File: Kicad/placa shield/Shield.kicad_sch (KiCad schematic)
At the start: 22 parts, among them J1 HC-05 connector, J2 Digital/PWM, J3 Power, J4 Analog, J5 Digital/PWM, J6 Dimmer module, SW1 SW_Push, SW2 SW_Push, SW3 SW_Push, SW4 SW_Push, SW5 SW_DIP_x04, X3 ST-MORPHO-CN7, X4 ST-MORPHO-CN10

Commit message: previo a fabricación
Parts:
- removed R15, R16: 10k, Resistor_THT:R_Axial_DIN0207_L6.3mm_D2.5mm_P7.62mm_Horizontal, symbol Device:R
- removed SW3, SW4: SW_Push, Button_Switch_THT:SW_PUSH_6mm, symbol Switch:SW_Push
- RV1: value 1k -> 10k
- renumbered SW2 to Luz_OFF, SW1 to Luz_ON
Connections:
- net PA0 is gone; now on net A0: X3.28 (PA0)
- net PA1 is gone; now on net A1: X3.30 (PA1)
- net PA10 is gone; now on net 2: X4.33 (PA10)
- net PA2 is gone; now on net TX/1: X4.35 (PA2)
- net PA3 is gone; now on net RX/0: X4.37 (PA3)
- net PA9 is gone; now on net 8: X4.21 (PA9)
- net *10: now also X4.17 (PB6)
- net *11: now also X4.15 (PA7)
- net *3: now also X4.31 (PB3)
- net *5: now also X4.27 (PB4)
- net *6: now also X4.25 (PB10)
- net *9: now also X4.19 (PC7)
- net +3V3: now also Luz_OFF.2, Luz_ON.2, RV1.1, SW5.1, SW5.2, SW5.3, SW5.4
- net +5V: now also X3.18 (+5V); no longer Luz_OFF.2, Luz_ON.2, RV1.1, SW5.1, SW5.2, SW5.3, SW5.4
- net 12: now also X4.13 (PA6)
- net 13: now also X4.11 (PA5)
- net 4: now also X4.29 (PB5)
- net 7: now also X4.23 (PA8)
- net A2: now also X3.32 (PA4)
- net A3: now also X3.34 (PB0)
- net AGND: no longer X3.20 (GND), X3.22 (GND), X3.8 (GND), X4.20 (GND)
- net AREF: now also X4.7 (AVDD)
- net GND: now also X3.20 (GND), X3.22 (GND)
- net IOREF: now also X3.12 (IOREF)
- net SCL/A5: now also X3.38 (PC0/PB8), X4.3 (PB8)
- net SDA/A4: now also X3.36 (PC1/PB9), X4.5 (PB9)
- net VCC: now also X3.24 (VIN)
- net ~{RESET}: now also X3.14 (RESET)
- net +5V0: no longer names the net of X3.6 (E5V)
- net PA11: no longer names the net of X4.14 (PA11)
- net PA12: no longer names the net of X4.12 (PA12)
- net PB12: no longer names the net of X4.16 (PB12)
- net PB13: no longer names the net of X4.30 (PB13)
- net PB14: no longer names the net of X4.28 (PB14)
- net PB15: no longer names the net of X4.26 (PB15)
- net U5V: no longer names the net of X4.8 (U5V)
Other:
- moved on the sheet: RV1, X4

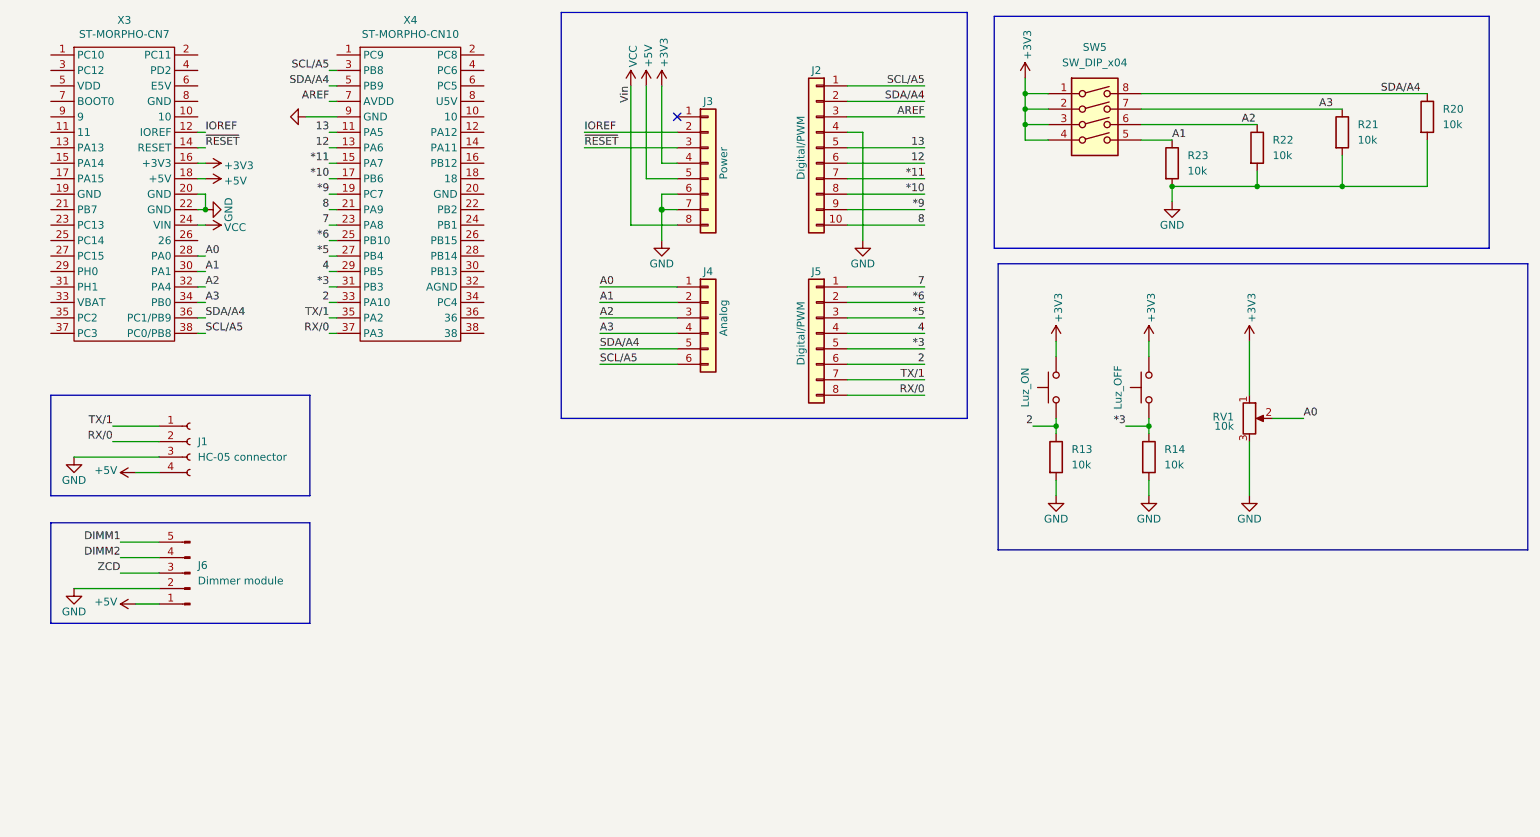
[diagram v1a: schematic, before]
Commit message: esquema shield actualizado con ínout final
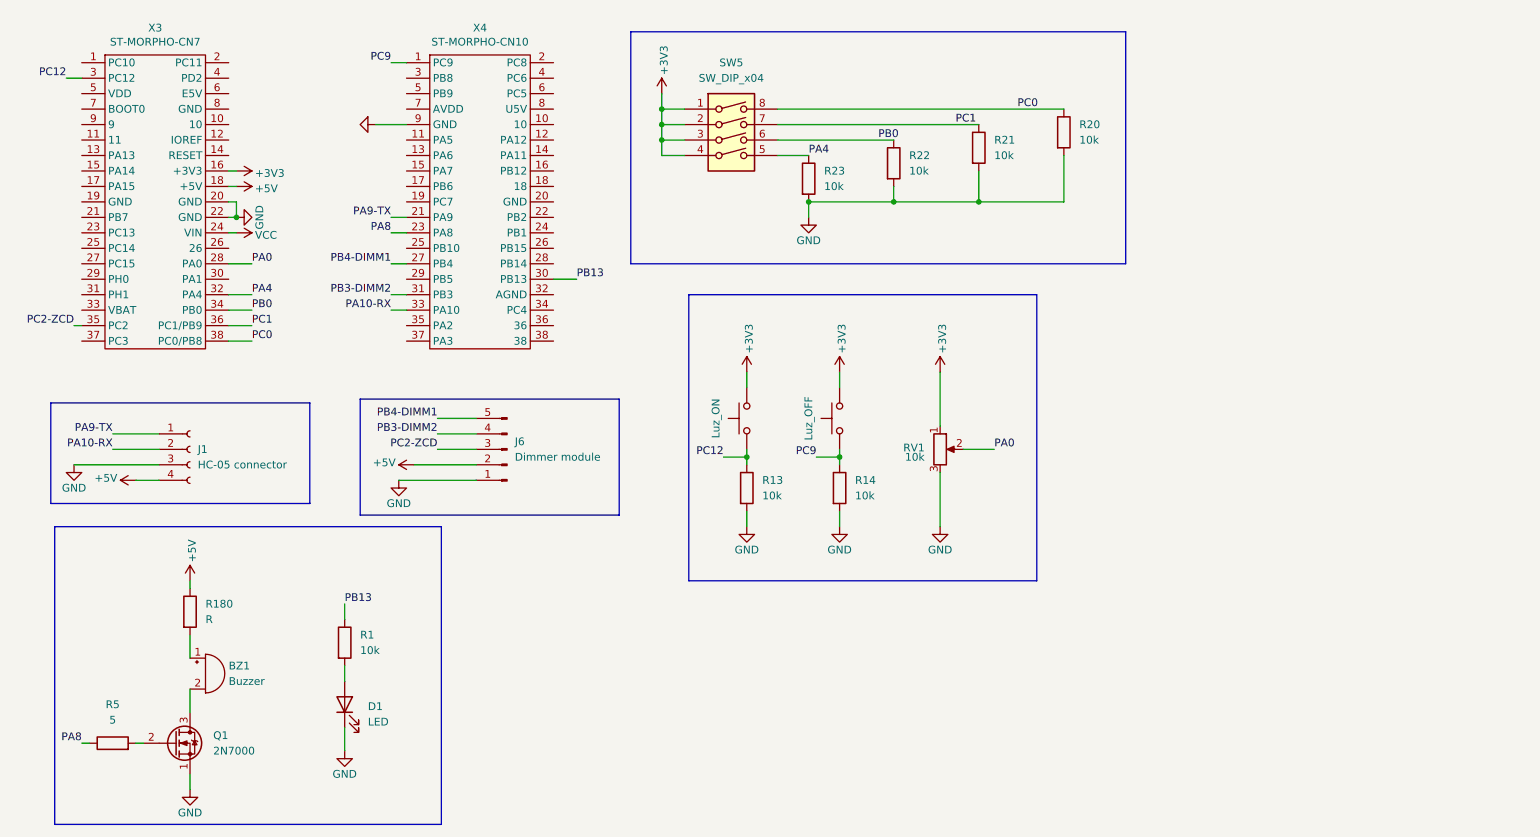
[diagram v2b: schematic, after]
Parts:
- removed J2: Digital/PWM, Connector_PinSocket_2.54mm:PinSocket_1x10_P2.54mm_Vertical, symbol Connector_Generic:Conn_01x10
- removed J3: Power, Connector_PinSocket_2.54mm:PinSocket_1x08_P2.54mm_Vertical, symbol Connector_Generic:Conn_01x08
- removed J4: Analog, Connector_PinSocket_2.54mm:PinSocket_1x06_P2.54mm_Vertical, symbol Connector_Generic:Conn_01x06
- removed J5: Digital/PWM, Connector_PinSocket_2.54mm:PinSocket_1x08_P2.54mm_Vertical, symbol Connector_Generic:Conn_01x08
- added BZ1: Buzzer, symbol Device:Buzzer
- added D1: LED, symbol Device:LED
- added Q1: 2N7000, Package_TO_SOT_THT:TO-92_Inline, symbol Transistor_FET:2N7000
- added R1: 10k, symbol Device:R
- added R180: R, symbol Device:R
- added R5: 5, symbol Device:R
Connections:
- net DIMM1 is gone; now on net PB4-DIMM1: J6.5 (Pin_5)
- net ZCD is gone; now on net PC2-ZCD: J6.3 (Pin_3)
- net +5V: now also J6.2 (Pin_2), R180.1; no longer J6.1 (Pin_1)
- net GND: now also J6.1 (Pin_1), D1.1 (K), Q1.1 (S); no longer J6.2 (Pin_2)
- net PC12: now reaches X3.3 (PC12)
- net PC12: now also Luz_ON.1, R13.1
- net PC2-ZCD: now reaches X3.35 (PC2)
- net PC9: now reaches X4.1 (PC9)
- net PC9: now also Luz_OFF.1, R14.1
- net PB13: now reaches X4.30 (PB13)
- net PB13: now also R1.1
- net *10: no longer names the net of X4.17 (PB6)
- net *11: no longer names the net of X4.15 (PA7)
- removed net *3: Luz_OFF.1, R14.1, X4.31 (PB3)
- net *5 renamed PB4-DIMM1
- net *6: no longer names the net of X4.25 (PB10)
- net *9: no longer names the net of X4.19 (PC7)
- net 12: no longer names the net of X4.13 (PA6)
- net 13: no longer names the net of X4.11 (PA5)
- removed net 2: Luz_ON.1, R13.1, X4.33 (PA10)
- net 4: no longer names the net of X4.29 (PB5)
- net 7 renamed PA8
- net PA8: now also R5.1
- net 8 renamed PA9-TX
- net PA9-TX: now also J1.1 (Pin_1)
- net A0 renamed PA0
- net A1 renamed PA4
- net PA4: now also X3.32 (PA4); no longer X3.30 (PA1)
- net A2 renamed PB0
- net PB0: now also X3.34 (PB0); no longer X3.32 (PA4)
- net A3 renamed PC1
- net PC1: now also X3.36 (PC1/PB9); no longer X3.34 (PB0)
- net AREF: no longer names the net of X4.7 (AVDD)
- net DIMM2 renamed PB3-DIMM2
- net PB3-DIMM2: now also X4.31 (PB3)
- net IOREF: no longer names the net of X3.12 (IOREF)
- net RX/0: no longer names the net of X4.37 (PA3)
- net RX/0: no longer J1.2 (Pin_2)
- net SCL/A5: no longer names the net of X4.3 (PB8)
- net SCL/A5: no longer X3.38 (PC0/PB8)
- net SDA/A4 renamed PC0
- net PC0: now also X3.38 (PC0/PB8); no longer X3.36 (PC1/PB9), X4.5 (PB9)
- net TX/1: no longer names the net of X4.35 (PA2)
- net TX/1: no longer J1.1 (Pin_1)
- net ~{RESET}: no longer names the net of X3.14 (RESET)
- new net: Q1.2 (G), R5.2
- new net: BZ1.2 (-), Q1.3 (D)
- new net: BZ1.1 (+), R180.2
- new net: D1.2 (A), R1.2
- new net PA10-RX: J1.2 (Pin_2), X4.33 (PA10)
- no-connect marks 1 -> 0
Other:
- title: (none) -> Esquemático del shield del proyecto final
- moved on the sheet: J1, J6, Luz_OFF, Luz_ON, R13, R14, R20, R21, R22, R23, RV1, SW5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
